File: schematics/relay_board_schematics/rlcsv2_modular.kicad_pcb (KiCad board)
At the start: 2 copper layers, 45 x 75 mm, 31 parts, among them P1 ACT_PWR, P2 CONN_01X09, P3 ACTUATOR, Q1 MMBF170, Q2 MMBF170, U1 SPST_POWER_RELAY, U2 dpdt_relay, U3 INA180A1, U4 INA180A1

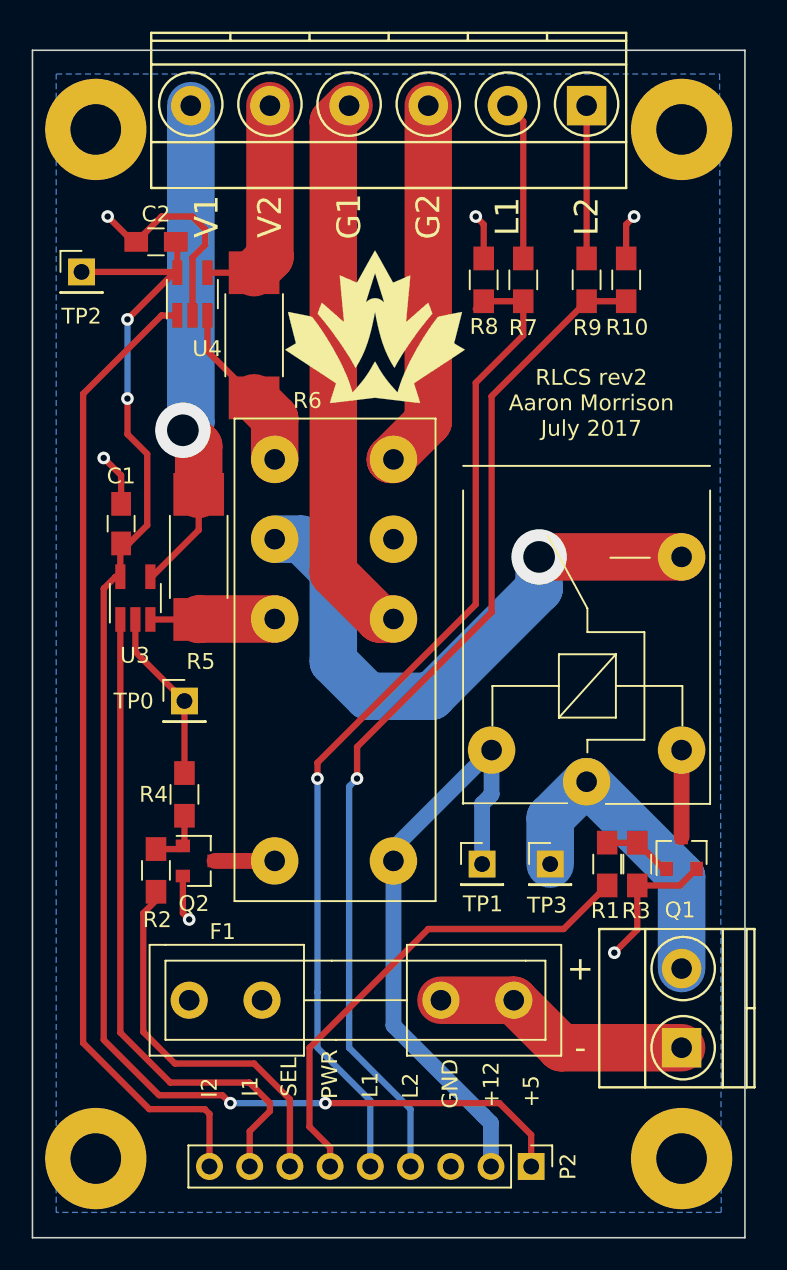
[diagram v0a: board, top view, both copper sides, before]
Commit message: Change fusing from bottom side to top side
Correct that error. Also add flyback diode to relay board
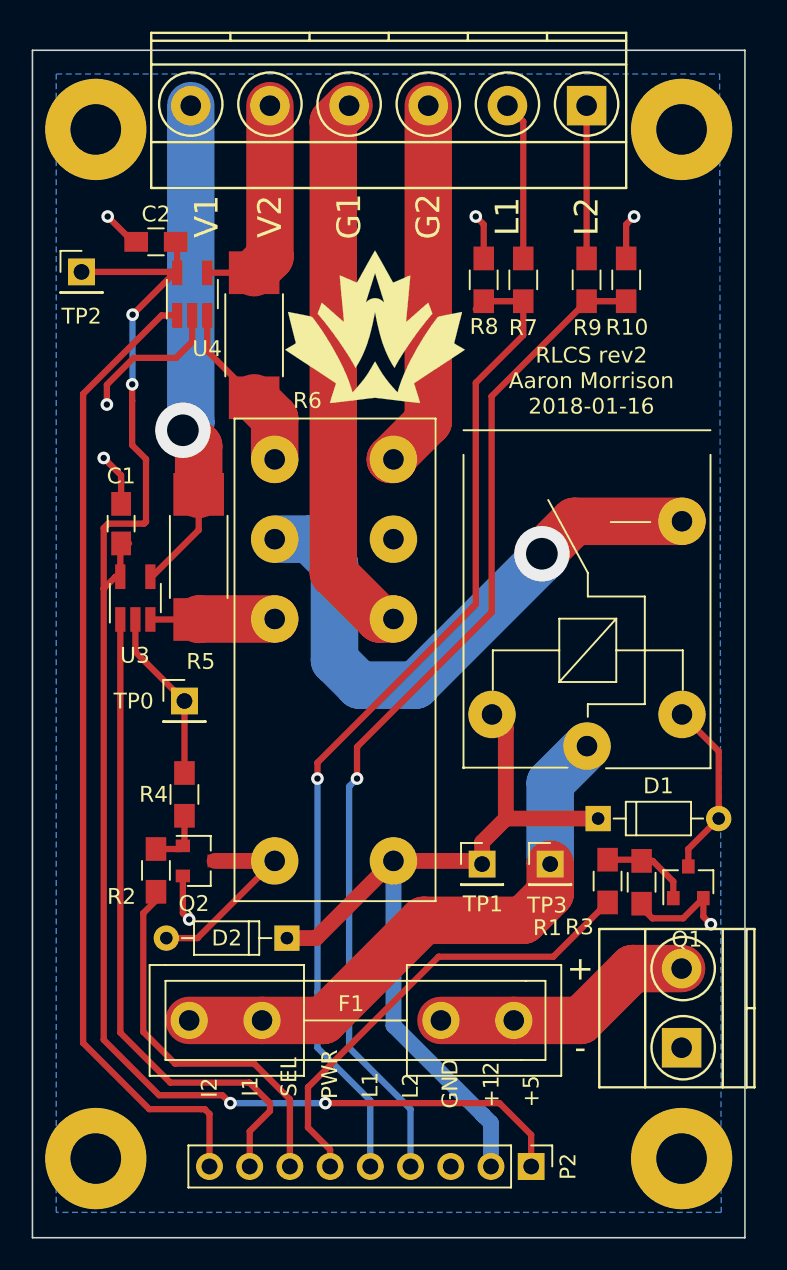
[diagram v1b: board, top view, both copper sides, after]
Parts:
- added D1: D, Diodes_THT:D_DO-35_SOD27_P7.62mm_Horizontal, F.Cu at (85.7, 123.5)
- added D2: D, Diodes_THT:D_DO-35_SOD27_P7.62mm_Horizontal, F.Cu at (66.1, 131.1)
- moved U1 2.25 mm to (85.0, 119.0)
- moved Q1 1.90 mm to (91.4, 127.5)
- moved F1 1.28 mm to (80.4, 136.3)
- moved R3 1.18 mm to (88.5, 127.5)
- moved R1 1.08 mm to (86.3, 127.5)
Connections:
- F1 pad 2: GND -> /Relays/VIN
- P1 pad 1: Net-(F1-Pad1) -> GND
- P1 pad 2: /Relays/VIN -> Net-(F1-Pad1)
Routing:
- net /Relays/VIN: track 20.4 -> 36.4 mm
- net +12V: track 38.9 -> 53.3 mm
- net Net-(D2-Pad2): track 3.80 -> 12.7 mm
- net Net-(D1-Pad2): track 5.50 -> 11.4 mm
- net +5V: track 92.6 -> 97.3 mm
- net GND: track 45.7 -> 41.8 mm, vias 6 -> 7
- net POWER: track 31.1 -> 29.3 mm
- net Net-(Q1-Pad1): track 4.63 -> 5.77 mm
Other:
- board text added: "RLCS rev2 Aaron Morrison 2018-01-16"
- board text removed: "RLCS rev2 Aaron Morrison July 2017"
